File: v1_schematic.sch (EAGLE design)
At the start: 124 parts, among them IC1 PCA82C250, IC2 FT232RL, IC3 SP3223EBP, IC4 MAX481CPA, IC5 LM2576T, Q1 25MHz, Q2 32.768kHz, Q3 2N2222A, T1 ST02-3.5MM, T3 2N2222, T4 2N2222, T5 2N2222, T6 2N2222, T7 2N2222, U1 ON_SEMICONDUCTOR_NCP1117ST33T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, U2 ON_SEMICONDUCTOR_NCP1117ST50T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, X1 MINI-USB-32005-201, X6 SDBMF, X7 5566-8, X8 5566-8

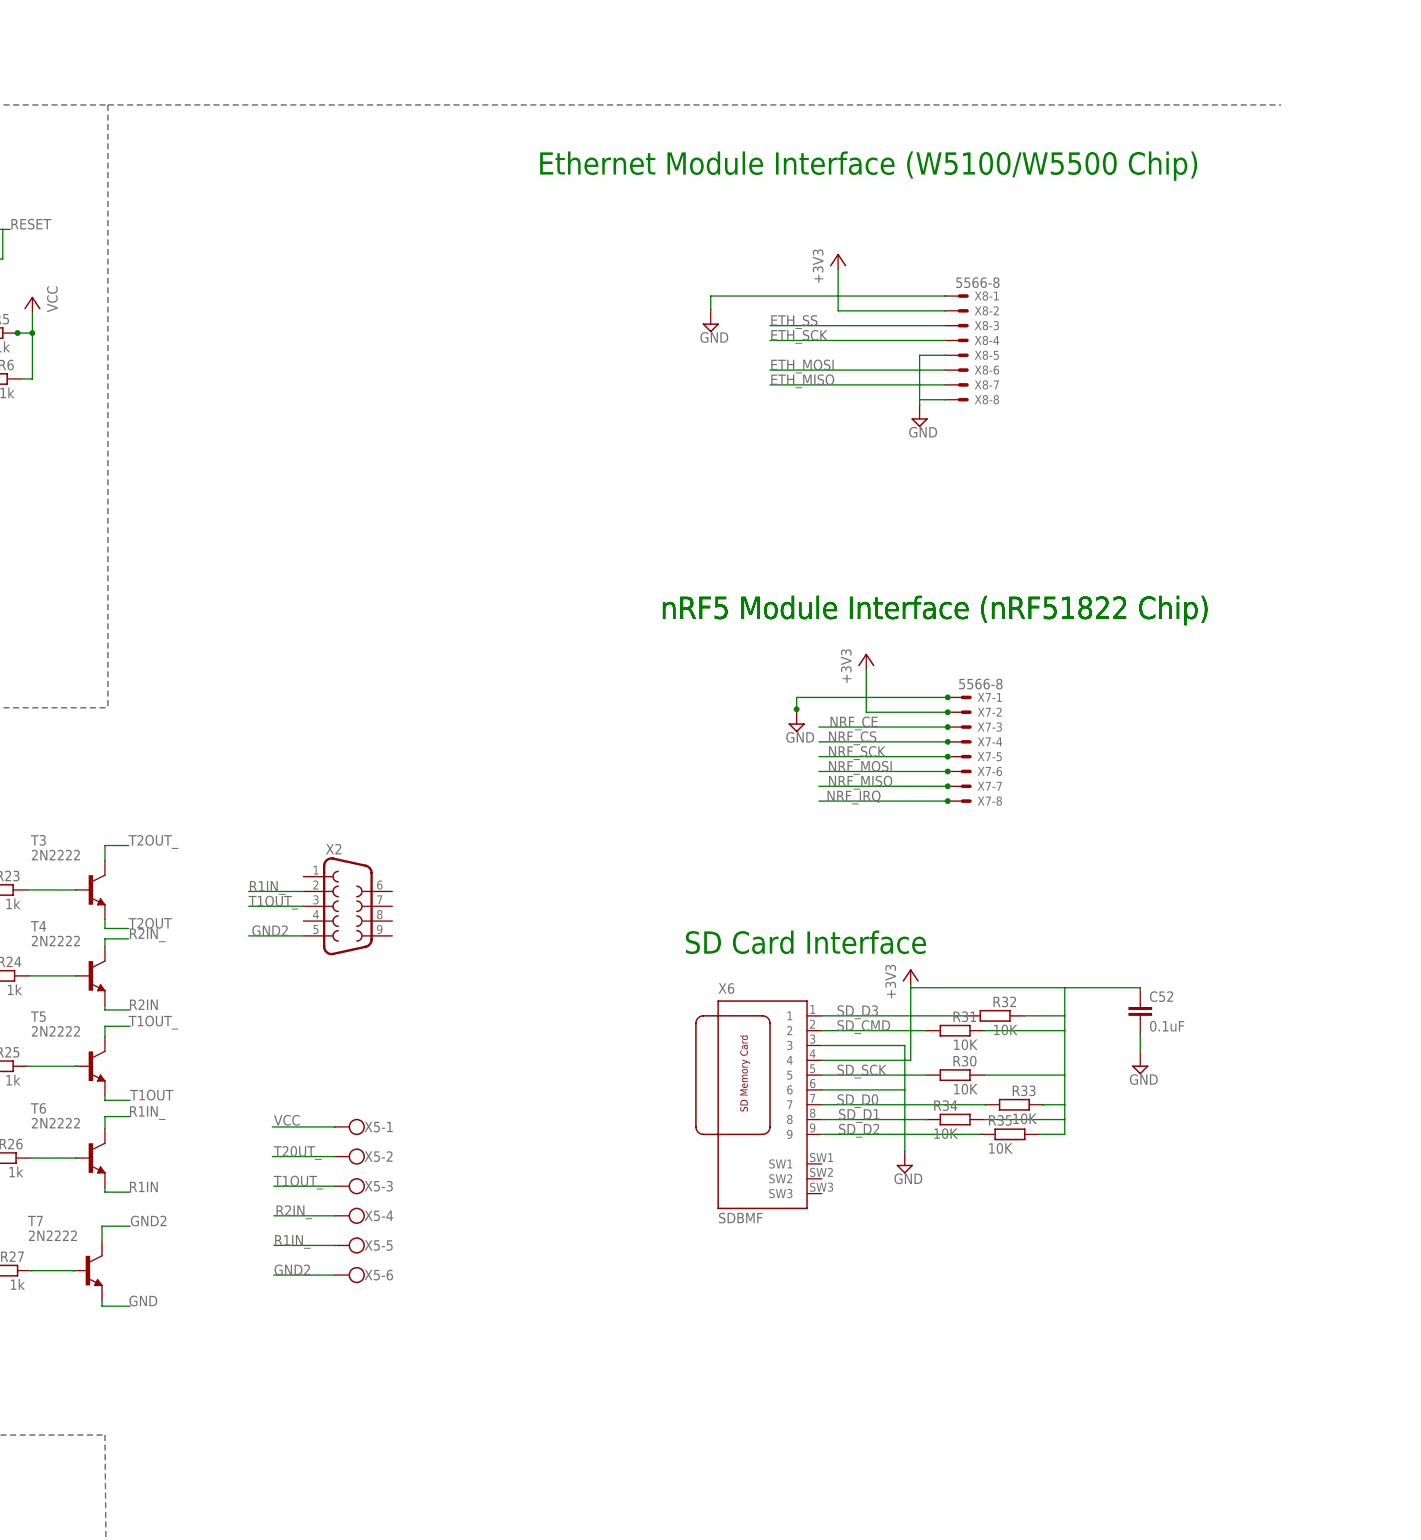
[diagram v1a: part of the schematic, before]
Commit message: Organization
- Minor adjustments to arrangement
- Added reference schematic for STMF4VEx
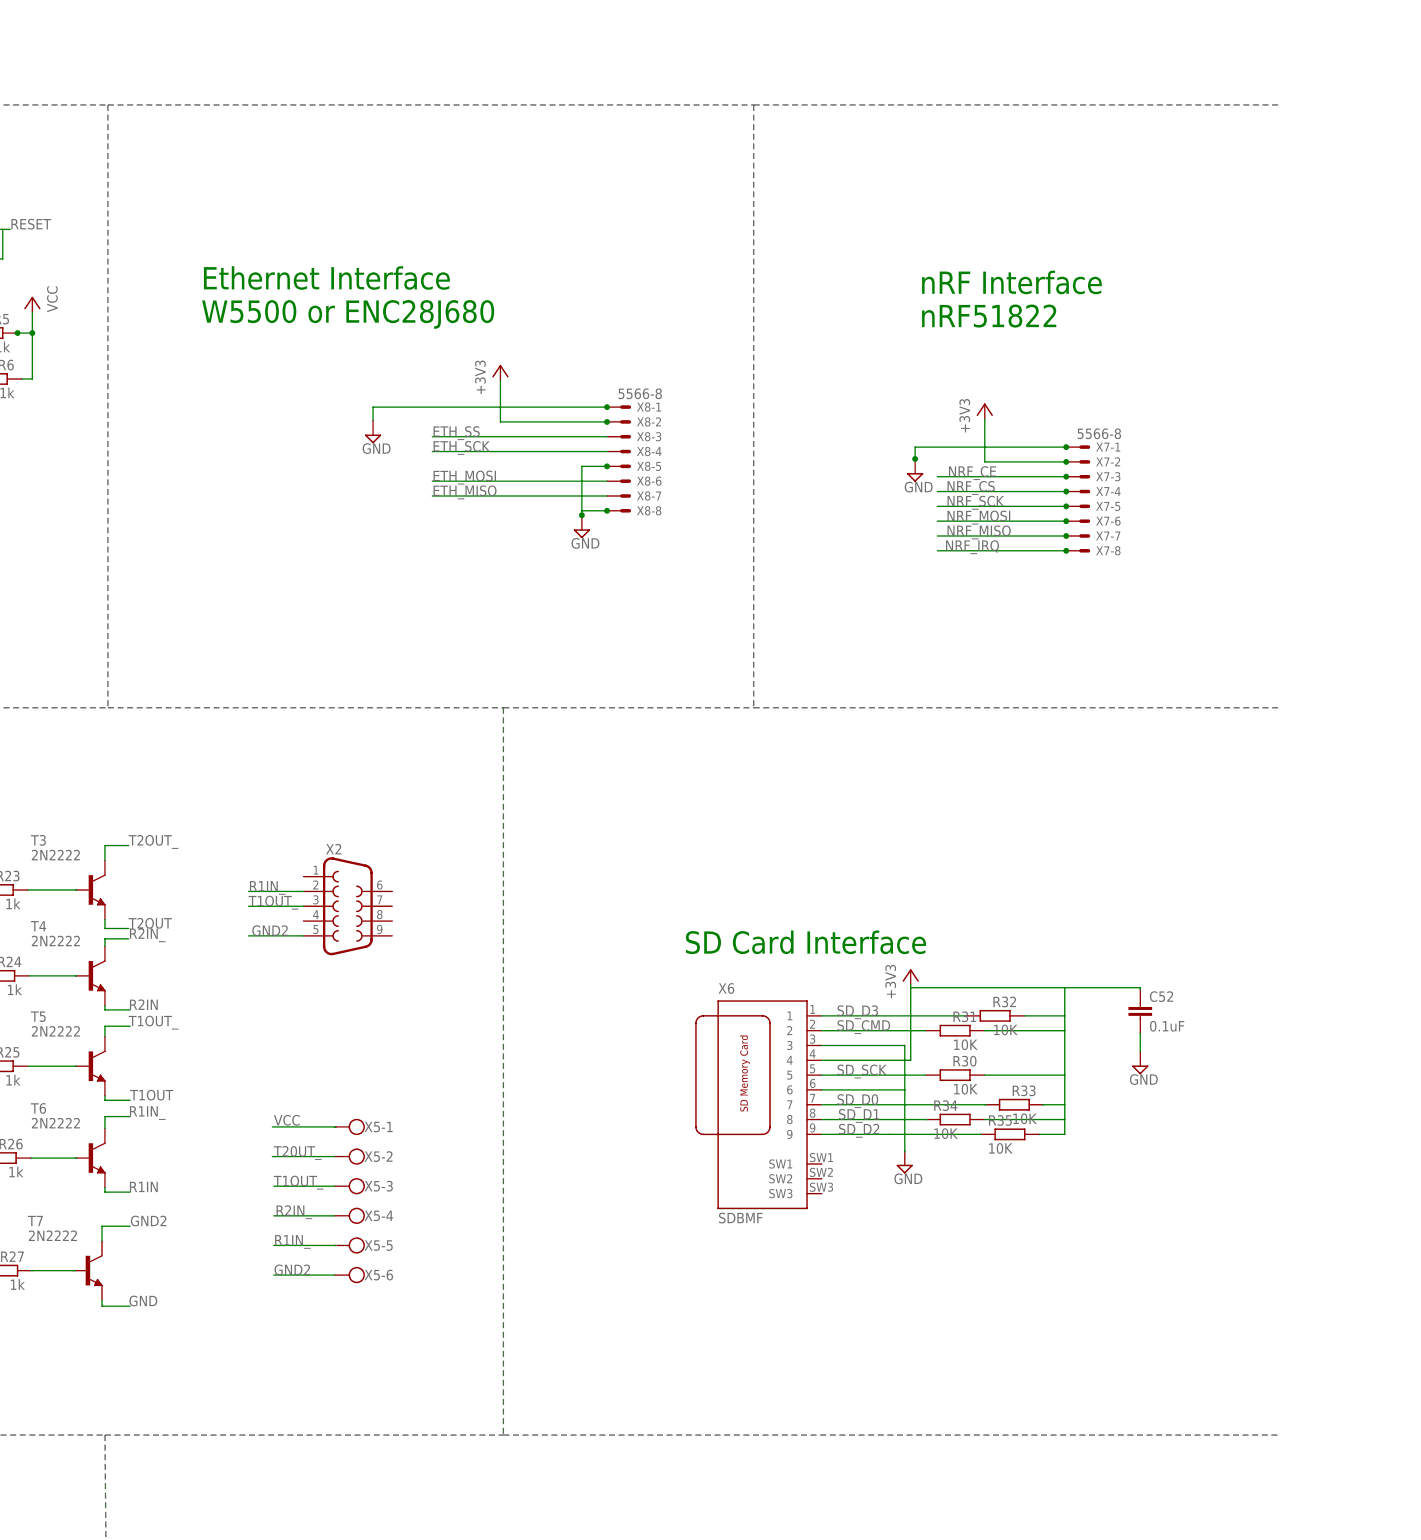
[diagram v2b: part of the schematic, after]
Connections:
- net +3V3: now also X8-2.S
- net GND: now also X8-1.S, X8-5.S, X8-8.S
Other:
- note added: "Ethernet Interface W5500 or ENC28J680"
- note added: "nRF Interface nRF51822"
- note removed: "Ethernet Module Interface (W5100/W5500 Chip)"
- note removed: "nRF5 Module Interface (nRF51822 Chip)"
- moved on the sheet: X7-1, X7-2, X7-3, X7-4, X7-5, X7-6, X7-7, X7-8, X8-1, X8-2, X8-3, X8-4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

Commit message: GPIOs
- Added input and output GPIO interfaces
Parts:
- added DIR1, DIR10, DIR2, DIR3, DIR4, DIR5, DIR6, DIR7, DIR8, DIR9, NPN1, NPN10, NPN2, NPN3, NPN4, NPN5, NPN6, NPN7, NPN8, NPN9, PNP1, PNP10, PNP2, PNP3, PNP4, PNP5, PNP6, PNP7, PNP8, PNP9, SJ1, SJ2, SJ3, SJ4, SJ5, SJ6: (no value), jumper:SJ2WW
- added R36, R37, R38, R39, R40, R41, R42, R43, R44, R45, R46, R47, R48, R49, R50, R51: 220R, rcl:R-EU_R0805
- added X10, X11, X12, X13, X14, X15, X16, X17, X18, X19, X20, X21, X22, X23, X24, X9: PC817SW, GadgetFactory_v1:PC817SW
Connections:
- new net N$1: PNP1.2, R37.2
- new net N$100: NPN5.1
- new net N$101: PNP9.2, R45.2
- new net N$102: DIR5.2, X14.COL
- new net N$103: R45.1, X18.A
- new net N$104: DIR5.1
- new net N$105: DIR5.3
- new net N$106: PNP6.2, R42.2
- new net N$107: R42.1, X15.A
- new net N$108: NPN6.2, X15.C
- new net N$109: PNP6.3
- new net N$110: NPN6.1
- new net N$111: NPN9.2, X18.C
- new net N$112: DIR6.2, X15.COL
- new net N$113: PNP9.3
- new net N$114: DIR6.1
- new net N$115: DIR6.3
- new net N$116: PNP7.2, R43.2
- new net N$117: R43.1, X16.A
- new net N$118: NPN7.2, X16.C
- new net N$119: PNP7.3
- new net N$120: NPN7.1
- new net N$121: NPN9.1
- new net N$122: DIR7.2, X16.COL
- new net N$123: DIR9.2, X18.COL
- new net N$124: DIR7.1
- new net N$125: DIR7.3
- new net N$126: DIR9.1
- new net N$127: DIR9.3
- new net N$128: PNP10.2, R46.2
- new net N$129: R46.1, X19.A
- new net N$130: NPN10.2, X19.C
- new net N$131: PNP10.3
- new net N$132: NPN10.1
- new net N$133: DIR10.2, X19.COL
- new net N$134: DIR10.1
- new net N$135: DIR10.3
- new net N$136: R47.1, X20.A
- new net N$137: X20.COL
- new net N$138: X20.EMIT
- new net N$139: SJ1.1
- new net N$140: SJ1.3
- new net N$141: R48.2, SJ2.2
- new net N$142: R48.1, X21.A
- new net N$143: X21.COL
- new net N$144: X21.EMIT
- new net N$145: SJ2.1
- new net N$146: SJ2.3
- new net N$147: R49.2, SJ3.2
- new net N$148: R49.1, X22.A
- new net N$149: X22.COL
- new net N$150: X22.EMIT
- new net N$151: SJ3.1
- new net N$152: SJ3.3
- new net N$153: R50.2, SJ5.2
- new net N$154: R50.1, X23.A
- new net N$155: X23.COL
- new net N$156: X23.EMIT
- new net N$157: SJ5.1
- new net N$158: SJ5.3
- new net N$159: R51.2, SJ6.2
- new net N$160: R51.1, X24.A
- new net N$161: X24.COL
- new net N$162: X24.EMIT
- new net N$163: SJ6.1
- new net N$164: SJ6.3
- new net N$33: NPN1.2, X9.C
- new net N$37: PNP1.3
- new net N$38: NPN1.1
- new net N$39: PNP8.2, R44.2
- new net N$47: DIR1.2, X9.COL
- new net N$48: R44.1, X17.A
- new net N$55: R27.1, T7.B
- new net N$57: DIR1.1
- new net N$58: DIR1.3
- new net N$59: R36.2, SJ4.2
- new net N$60: R36.1, X10.A
- new net N$61: R47.2, SJ1.2
- new net N$62: X10.COL
- new net N$63: X10.EMIT
- new net N$64: SJ4.1
- new net N$65: SJ4.3
- new net N$66: PNP2.2, R38.2
- new net N$67: R38.1, X11.A
- new net N$68: NPN2.2, X11.C
- new net N$69: PNP2.3
- new net N$70: NPN2.1
- new net N$71: NPN8.2, X17.C
- new net N$72: DIR2.2, X11.COL
- new net N$73: PNP8.3
- new net N$74: DIR2.1
- new net N$75: DIR2.3
- new net N$76: PNP3.2, R39.2
- new net N$77: R39.1, X12.A
- new net N$78: NPN3.2, X12.C
- new net N$79: PNP3.3
- new net N$80: NPN3.1
- new net N$81: NPN8.1
- new net N$82: DIR3.2, X12.COL
- new net N$83: DIR8.2, X17.COL
- new net N$84: DIR3.1
- new net N$85: DIR3.3
- new net N$86: PNP4.2, R40.2
- new net N$87: R40.1, X13.A
- new net N$88: NPN4.2, X13.C
- new net N$89: PNP4.3
- new net N$90: NPN4.1
- new net N$91: DIR8.1
- new net N$92: DIR4.2, X13.COL
- new net N$93: DIR8.3
- new net N$94: DIR4.1
- new net N$95: DIR4.3
- new net N$96: PNP5.2, R41.2
- new net N$97: R41.1, X14.A
- new net N$98: NPN5.2, X14.C
- new net N$99: PNP5.3
- net +12V: now also IC5.FB
- net +3V3: now also C17.1, C23.1, C26.1, C32.1, C45.+, PNP1.1, PNP10.1, PNP2.1, PNP3.1, PNP4.1, PNP5.1, PNP6.1, PNP7.1, PNP8.1, PNP9.1, R23.2, R26.2, R27.2, R33.1
- net GND: now also C14.1, NPN1.3, NPN10.3, NPN2.3, NPN3.3, NPN4.3, NPN5.3, NPN6.3, NPN7.3, NPN8.3, NPN9.3, R28.1, X10.C, X11.EMIT, X12.EMIT, X13.EMIT, X14.EMIT, X15.EMIT, X16.EMIT, X17.EMIT, X18.EMIT, X19.EMIT, X20.C, X21.C, X22.C, X23.C, X24.C, X6.3, X6.6, X9.EMIT
- net N$31: now also R37.1, X9.A; no longer X6.3, X6.6
- net N$49: now also T3.B
- net N$51: now also T4.B
- net N$52: now also T5.B
- net N$54: now also T6.B
- net R1IN: now also R21.2
- net R2IN: now also R20.2
- net SD_D0: now also R33.2
- net SD_D1: now also R34.1
- net SD_D2: now also R35.1
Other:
- note added: "GPIOs - Input Sensors"
- note added: "GPIOs - Output Actuators"
- moved on the sheet: C1, C10, C11, C12, C13, C14, C15, C16, C17, C18, C19, C2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

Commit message: GPIOs
- Added terminals for GPIO connection
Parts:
- added JP1: (no value), jumper:JP2W
- added X25, X26, X27, X28, X29, X30, X31, X32, X33, X34: (no value), con-wago-500:W237-103
- added X35, X36, X37, X38, X39, X40: (no value), con-wago-500:W237-102
- renumbered SJ1 to DIR12, SJ2 to DIR13, SJ3 to DIR14, SJ4 to DIR11, SJ5 to DIR15, SJ6 to DIR16
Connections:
- net N$138 renamed COM2
- net N$144 renamed COM3
- net N$162 renamed COM6
- net N$63 renamed COM1
- removed net N$100: NPN5.1
- removed net N$105: DIR5.3
- removed net N$109: PNP6.3
- removed net N$110: NPN6.1
- removed net N$113: PNP9.3
- removed net N$115: DIR6.3
- removed net N$119: PNP7.3
- removed net N$120: NPN7.1
- removed net N$121: NPN9.1
- removed net N$125: DIR7.3
- removed net N$127: DIR9.3
- removed net N$131: PNP10.3
- removed net N$132: NPN10.1
- removed net N$135: DIR10.3
- removed net N$137: X20.COL
- removed net N$140: DIR12.3
- removed net N$143: X21.COL
- removed net N$146: DIR13.3
- removed net N$149: X22.COL
- removed net N$150: X22.EMIT
- removed net N$152: DIR14.3
- removed net N$155: X23.COL
- removed net N$156: X23.EMIT
- removed net N$158: DIR15.3
- removed net N$161: X24.COL
- removed net N$164: DIR16.3
- removed net N$58: DIR1.3
- removed net N$62: X10.COL
- removed net N$65: DIR11.3
- removed net N$69: PNP2.3
- removed net N$70: NPN2.1
- removed net N$73: PNP8.3
- removed net N$75: DIR2.3
- removed net N$79: PNP3.3
- removed net N$80: NPN3.1
- removed net N$81: NPN8.1
- removed net N$85: DIR3.3
- removed net N$89: PNP4.3
- removed net N$90: NPN4.1
- removed net N$93: DIR8.3
- removed net N$95: DIR4.3
- removed net N$99: PNP5.3
- new net COM4: X22.EMIT, X38-2.KL
- new net COM5: X23.EMIT, X39-2.KL
- new net IN1: DIR1.3, NPN1.1, PNP1.3
- new net IN10: DIR10.3, NPN10.1, PNP10.3
- new net IN2: DIR2.3, NPN2.1, PNP2.3, X26-2.KL
- new net IN3: DIR3.3, NPN3.1, PNP3.3, X27-2.KL
- new net IN4: DIR4.3, NPN4.1, PNP4.3
- new net IN5: DIR5.3, NPN5.1, PNP5.3
- new net IN6: DIR6.3, NPN6.1, PNP6.3
- new net IN7: DIR7.3, NPN7.1, PNP7.3
- new net IN8: DIR8.3, NPN8.1, PNP8.3
- new net IN9: DIR9.3, NPN9.1, PNP9.3, X33-2.KL
- new net OUT1: DIR11.3, X10.COL
- new net OUT2: DIR12.3, X20.COL
- new net OUT3: DIR13.3, X21.COL
- new net OUT4: DIR14.3, X22.COL, X38-1.KL
- new net OUT5: DIR15.3, X23.COL, X39-1.KL
- new net OUT6: DIR16.3, X24.COL
- net +12V: now also JP1.1
- net GND: now also X26-1.KL, X29-1.KL, X33-1.KL
- net N$37: now also JP1.3; no longer PNP1.3
- net N$38: now also JP1.2, X26-3.KL, X28-3.KL, X29-3.KL, X33-3.KL, X34-3.KL; no longer NPN1.1

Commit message: Updates
- Completed GPIO-MCU connection
- Changed labels to tags for easier visibility
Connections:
- net A1 renamed PE3
- net A2 renamed PE2
- net A3 renamed PE1
- net A4 renamed PE0
- net B1 renamed PE4
- net B2 renamed PE5
- net B3 renamed PE6
- net B4 renamed PB9
- net D15 renamed PA10
- net E1 renamed PC14
- net E15 renamed PA9
- net F1 renamed PC15
- net F15 renamed PA8
- net G1 renamed PH0
- net G15 renamed PC7
- net H1 renamed PH1
- net L14 renamed PD15
- net M14 renamed PD14
- net M15 renamed PD13
- net N$26 renamed VBAT
- net N$5 renamed PE14
- net N$6 renamed PE15
- net N11 renamed PE13
- net P10 renamed PE11
- net P8 renamed PE8
- net P9 renamed PE9
- net R10 renamed PE12
- net R8 renamed PE7
- net R9 renamed PE10
- removed net A11: U$1.PD7
- removed net B12: U$1.PD0
- removed net C12: U$1.PD1
- removed net D1: U$1.PC13
- removed net H15: U$1.PC6
- removed net L4: U$1.PC3
- removed net M2: U$1.PC0
- removed net M3: U$1.PC1
- removed net M4: U$1.PC2
- removed net N$104: DIR5.1
- removed net N$114: DIR6.1
- removed net N$124: DIR7.1
- removed net N$126: DIR9.1
- removed net N$134: DIR10.1
- removed net N$139: DIR12.1
- removed net N$145: DIR13.1
- removed net N$151: DIR14.1
- removed net N$157: DIR15.1
- removed net N$163: DIR16.1
- removed net N$34: U$1.VSS, U$1.VSS1, U$1.VSS2, U$1.VSS3, U$1.VSSA
- removed net N$57: DIR1.1
- removed net N$64: DIR11.1
- removed net N$74: DIR2.1
- removed net N$84: DIR3.1
- removed net N$91: DIR8.1
- removed net N$94: DIR4.1
- removed net N13: U$1.PD12
- removed net N14: U$1.PD11
- removed net N15: U$1.PD10
- removed net N5: U$1.PC4
- removed net P14: U$1.PD9
- removed net P15: U$1.PD8
- removed net P5: U$1.PC5
- new net PC0: DIR1.1, U$1.PC0
- new net PC1: DIR2.1, U$1.PC1
- new net PC13: DIR8.1, U$1.PC13
- new net PC2: DIR3.1, U$1.PC2
- new net PC3: DIR4.1, U$1.PC3
- new net PC4: DIR5.1, U$1.PC4
- new net PC5: DIR6.1, U$1.PC5
- new net PC6: DIR7.1, U$1.PC6
- new net PD0: DIR9.1, U$1.PD0
- new net PD1: DIR10.1, U$1.PD1
- new net PD10: DIR14.1, U$1.PD10
- new net PD11: DIR15.1, U$1.PD11
- new net PD12: DIR16.1, U$1.PD12
- new net PD7: DIR11.1, U$1.PD7
- new net PD8: DIR12.1, U$1.PD8
- new net PD9: DIR13.1, U$1.PD9
- net COM1: now also X35-2.KL
- net COM2: now also X36-2.KL
- net COM3: now also X37-2.KL
- net COM6: now also X40-2.KL
- net GND: now also U$1.VSS, U$1.VSS1, U$1.VSS2, U$1.VSS3, U$1.VSSA, X25-1.KL, X27-1.KL, X28-1.KL, X30-1.KL, X31-1.KL, X32-1.KL, X34-1.KL
- net IN1: now also X25-2.KL
- net IN10: now also X34-2.KL
- net IN4: now also X28-2.KL
- net IN5: now also X29-2.KL
- net IN6: now also X30-2.KL
- net IN7: now also X31-2.KL
- net IN8: now also X32-2.KL
- net N$38: now also X25-3.KL, X27-3.KL, X30-3.KL, X31-3.KL, X32-3.KL
- net OUT1: now also X35-1.KL
- net OUT2: now also X36-1.KL
- net OUT3: now also X37-1.KL
- net OUT6: now also X40-1.KL
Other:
- moved on the sheet: C15, C16, DIR10, NPN10, PNP10, R46, X19, X25-1, X25-2, X25-3, X26-1, X26-2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

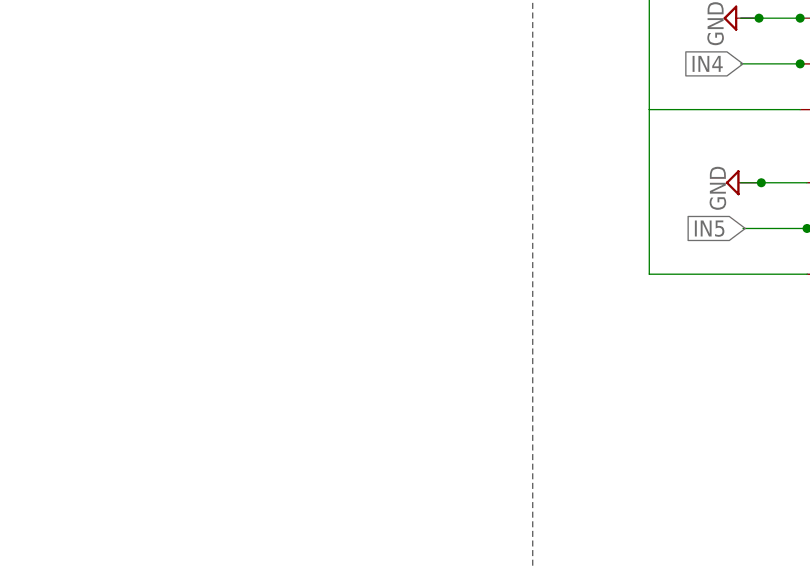
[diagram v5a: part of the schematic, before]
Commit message: Mount-Pads
Added mount Pads
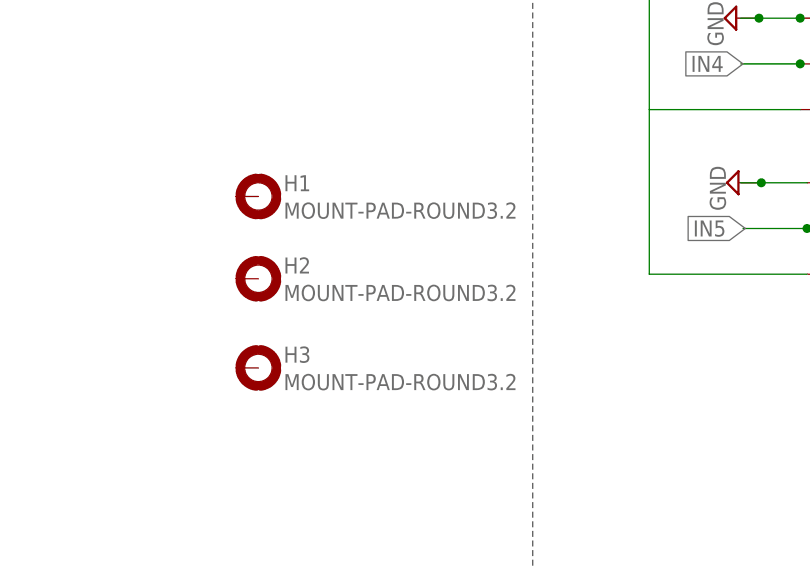
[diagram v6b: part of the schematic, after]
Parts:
- added H1, H2, H3: MOUNT-PAD-ROUND3.2, holes:MOUNT-PAD-ROUND3.2
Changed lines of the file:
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@@
 <part name="SUPPLY76" library="supply2" library_urn="urn:adsk.eagle:library:372" deviceset="GND" device=""/>
 <part name="SUPPLY77" library="supply2" library_urn="urn:adsk.eagle:library:372" deviceset="GND" device=""/>
+<part name="H1" library="holes" library_urn="urn:adsk.eagle:library:237" deviceset="MOUNT-PAD-ROUND" device="3.2" package3d_urn="urn:adsk.eagle:package:14282/1"/>
+<part name="H2" library="holes" library_urn="urn:adsk.eagle:library:237" deviceset="MOUNT-PAD-ROUND" device="3.2" package3d_urn="urn:adsk.eagle:package:14282/1"/>
+<part name="H3" library="holes" library_urn="urn:adsk.eagle:library:237" deviceset="MOUNT-PAD-ROUND" device="3.2" package3d_urn="urn:adsk.eagle:package:14282/1"/>
 </parts>
 <sheets>
@@
 <instance part="SUPPLY76" gate="GND" x="171.196" y="-100.838" rot="R270"/>
 <instance part="SUPPLY77" gate="GND" x="-211.582" y="54.102"/>
+<instance part="H1" gate="G$1" x="87.122" y="-177.8"/>
+<instance part="H2" gate="G$1" x="87.122" y="-186.944"/>
+<instance part="H3" gate="G$1" x="87.122" y="-196.85"/>
 </instances>
 <busses>
